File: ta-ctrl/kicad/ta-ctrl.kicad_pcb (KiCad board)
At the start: 4 copper layers, 45 x 45 mm, 0 parts

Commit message: all parts placed, about halfway through routing
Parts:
- added C1: 10nF, ta-ctrl:C_0603_1608Metric_ctrl_cpy, F.Cu at (138.1, 107.4)
- added C10: 100nF, ta-ctrl:C_0603_1608Metric_ctrl_cpy, F.Cu at (159.4, 94.4)
- added C11: 4pF, ta-ctrl:C_0402_1005Metric, F.Cu at (165.2, 100.9)
- added C12: 100nF, ta-ctrl:C_0603_1608Metric_ctrl_cpy, F.Cu at (159.4, 106.9)
- added C13: 4pF, ta-ctrl:C_0402_1005Metric, F.Cu at (163.8, 100.9)
- added C2: 100nF, ta-ctrl:C_0603_1608Metric_ctrl_cpy, F.Cu at (142.5, 107.3)
- added C3: 10uF, ta-ctrl:C_0603_1608Metric_ctrl_cpy, F.Cu at (144.8, 107.3)
- added C4: 100nF, ta-ctrl:C_0603_1608Metric_ctrl_cpy, F.Cu at (140.3, 107.4)
- added C5: 2.2uF, ta-ctrl:C_0603_1608Metric_ctrl_cpy, F.Cu at (172.2, 114.8)
- added C6: 10uF, ta-ctrl:C_0603_1608Metric_ctrl_cpy, F.Cu at (155.6, 92.3)
- added C7: 8pF, ta-ctrl:C_0402_1005Metric, F.Cu at (162.2, 97.2)
- added C8: 100nF, ta-ctrl:C_0603_1608Metric_ctrl_cpy, F.Cu at (148.3, 92.7)
- added C9: 8pF, ta-ctrl:C_0402_1005Metric, F.Cu at (159.6, 90.8)
- added D1: 3.3V, ta-ctrl:D_SOD-323F, F.Cu at (168.8, 102.8)
- added J1: PinSocket_16_ctrl, ta-ctrl:PinSocket_1x16_TartanArtibeus_ctrl_cpy, F.Cu at (155.0, 89.0)
- added J2: PinSocket_16_ctrl, ta-ctrl:PinSocket_1x16_TartanArtibeus_ctrl_cpy, F.Cu at (155.0, 127.0)
- added J3: MountingHole_ctrl, ta-ctrl:MountingHoles_TartanArtibeus_ctrl_cpy, F.Cu at (155.0, 108.0)
- added J4: PinSocket_4_ctrl, ta-ctrl:PinSocket_1x4_TartanArtibeus_ctrl_cpy, F.Cu at (135.9, 120.7)
- added J5: PinSocket_4_ctrl, ta-ctrl:PinSocket_1x4_TartanArtibeus_ctrl_cpy, F.Cu at (135.9, 95.3)
- added J6: PinSocket_5_ctrl, ta-ctrl:PinSocket_1x5_right_TartanArtibeus_ctrl_cpy, F.Cu at (174.1, 122.0)
- added J7: PinSocket_5_ctrl, ta-ctrl:PinSocket_1x5_left_TartanArtibeus_ctrl_cpy, F.Cu at (174.1, 94.0)
- added R1: DNP, ta-ctrl:R_0603_1608Metric_ctrl_cpy, F.Cu at (167.9, 117.4)
- added R10: DNP, ta-ctrl:R_0603_1608Metric_ctrl_cpy, F.Cu at (176.1, 109.0)
- added R11: DNP, ta-ctrl:R_0603_1608Metric_ctrl_cpy, F.Cu at (174.4, 108.9)
- added R12: DNP, ta-ctrl:R_0603_1608Metric_ctrl_cpy, F.Cu at (172.7, 108.9)
- added R13: 10K, ta-ctrl:R_0603_1608Metric_ctrl_cpy, F.Cu at (153.0, 109.7)
- added R14: 10K, ta-ctrl:R_0603_1608Metric_ctrl_cpy, F.Cu at (154.7, 109.7)
- added R15: 10k, ta-ctrl:R_0603_1608Metric_ctrl_cpy, F.Cu at (140.2, 92.7)
- added R16: DNP, ta-ctrl:R_0603_1608Metric_ctrl_cpy, F.Cu at (143.7, 92.7)
- added R17: 10k, ta-ctrl:R_0603_1608Metric_ctrl_cpy, F.Cu at (138.5, 92.7)
- added R18: DNP, ta-ctrl:R_0603_1608Metric_ctrl_cpy, F.Cu at (141.9, 92.7)
- added R19: DNP, ta-ctrl:R_0603_1608Metric_ctrl_cpy, F.Cu at (161.8, 116.5)
- added R2: DNP, ta-ctrl:R_0603_1608Metric_ctrl_cpy, F.Cu at (167.9, 115.8)
- added R3: DNP, ta-ctrl:R_0603_1608Metric_ctrl_cpy, F.Cu at (164.8, 124.9)
- added R4: DNP, ta-ctrl:R_0603_1608Metric_ctrl_cpy, F.Cu at (168.8, 124.9)
- added R5: DNP, ta-ctrl:R_0603_1608Metric_ctrl_cpy, F.Cu at (169.4, 91.6)
- added R6: DNP, ta-ctrl:R_0603_1608Metric_ctrl_cpy, F.Cu at (168.1, 98.8)
- added R7: DNP, ta-ctrl:R_0603_1608Metric_ctrl_cpy, F.Cu at (168.1, 100.4)
- added R8: DNP, ta-ctrl:R_0603_1608Metric_ctrl_cpy, F.Cu at (166.2, 91.6)
- added R9: DNP, ta-ctrl:R_0603_1608Metric_ctrl_cpy, F.Cu at (170.9, 108.9)
- added U1: LSF0204, ta-ctrl:TSSOP-14, F.Cu at (167.8, 121.3)
- added U2: LSF0204, ta-ctrl:TSSOP-14, F.Cu at (168.3, 95.2)
- added U3: LSF0204, ta-ctrl:TSSOP-14, F.Cu at (167.0, 109.2)
- added U4: LSM9DS1, ta-ctrl:LSM9DS1TR, F.Cu at (141.9, 101.2)
- added U5: HT-GPS200.20, ta-ctrl:HT-GPS200.20, F.Cu at (149.5, 116.3)
- added U6: MSP430FR5994IPM, ta-ctrl:MSP430FR5994IPM, F.Cu at (153.7, 100.7)
- added Y1: 32.768kHz, ta-ctrl:ECS327934QSTR, F.Cu at (162.3, 93.3)
- added Y2: 24MHz, ta-ctrl:ECX-1247, F.Cu at (162.2, 101.0)
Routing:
- net /Vdd: track 0.00 -> 134.2 mm, vias 0 -> 8
- net /EXP: track 0.00 -> 50.9 mm, vias 0 -> 1
- net /GNSS_TX: track 0.00 -> 44.4 mm
- net /GNSS_RX: track 0.00 -> 42.2 mm
- net /COMM: track 0.00 -> 42.2 mm, vias 0 -> 1
- net /Exp_CTS: track 0.00 -> 40.7 mm
- net /GNSS_PPS: track 0.00 -> 39.3 mm
- net /GNSS_nRST: track 0.00 -> 32.9 mm
- net /Comm_RX1_l: track 0.00 -> 30.8 mm, vias 0 -> 2
- net /Exp_TX: track 0.00 -> 30.4 mm
- net /Comm_TX1_l: track 0.00 -> 28.2 mm, vias 0 -> 2
- net /Comm_EN: track 0.00 -> 28.1 mm
- net /GNSS: track 0.00 -> 27.5 mm
- net /Exp_RX_l: track 0.00 -> 25.9 mm, vias 0 -> 2
- net /Exp_TX_l: track 0.00 -> 25.9 mm, vias 0 -> 2
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
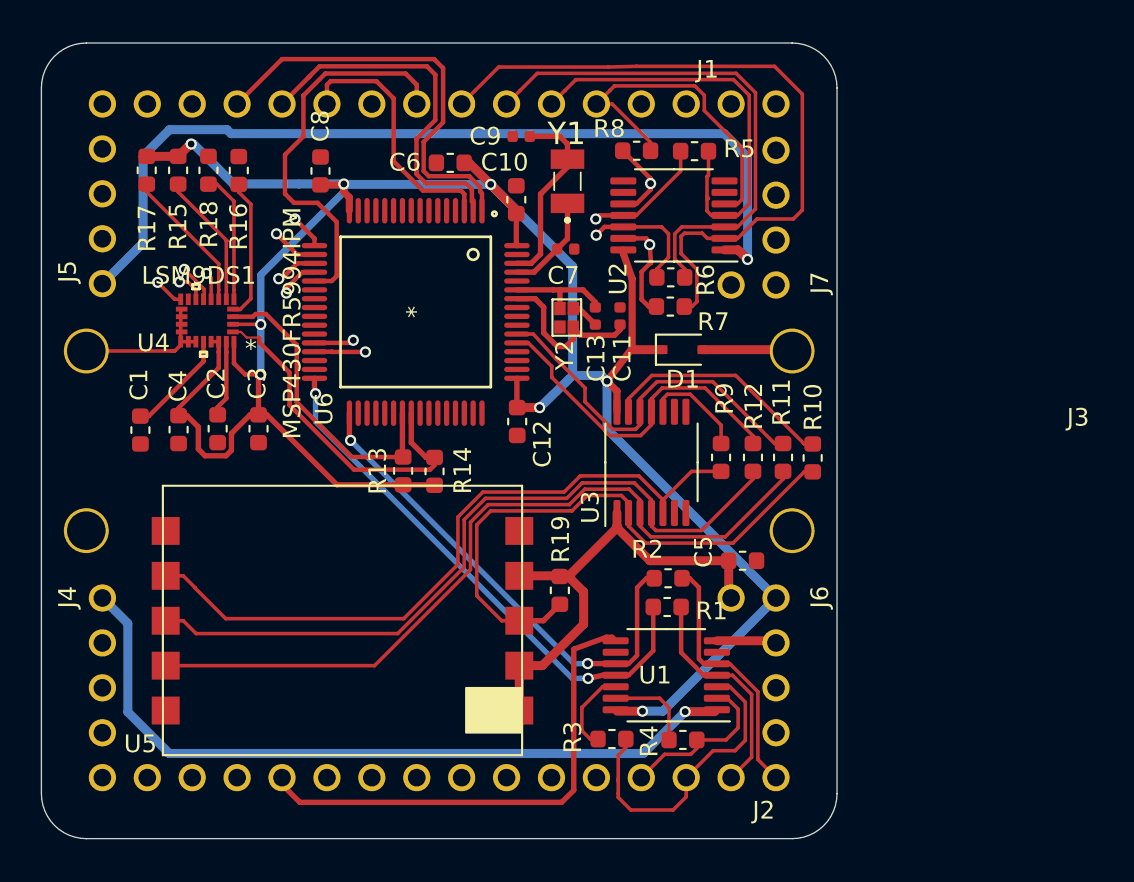
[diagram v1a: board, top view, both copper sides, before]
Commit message: done routing except ground connections
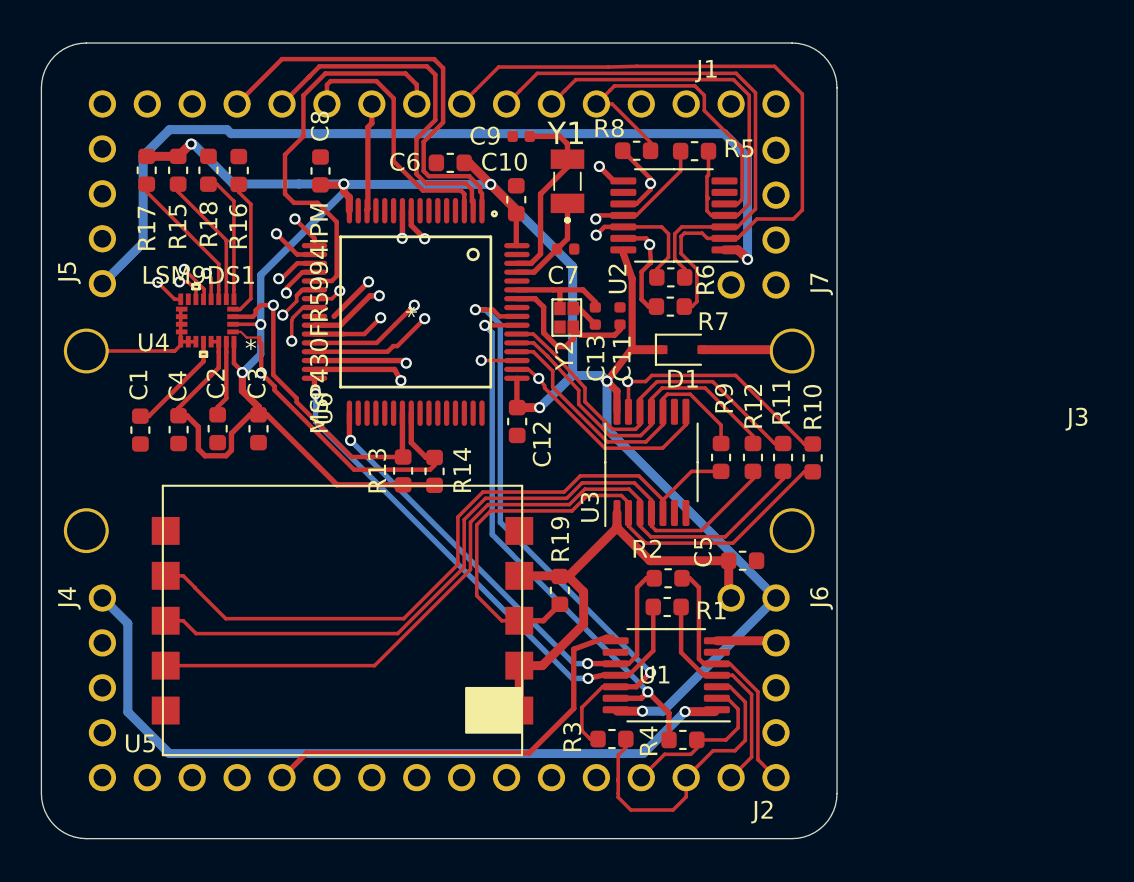
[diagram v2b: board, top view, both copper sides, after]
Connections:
- U6 pad 14: Net-(U6-Pad14) -> /Exp_RST
- U6 pad 22: Net-(U6-Pad22) -> /adc_int
- U6 pad 23: Net-(U6-Pad23) -> /Comm_EN
- U6 pad 24: /EXP_BOOT -> /Exp_EN
- U6 pad 25: /Comm_RST -> Net-(U6-Pad25)
- U6 pad 26: /GNSS_nRST_l -> /Comm_RST
- U6 pad 27: /GNSS_PPS_l -> /EXP_BOOT
- U6 pad 4: /Comm_EN -> Net-(U6-Pad4)
- U6 pad 44: /Exp_RST -> Net-(U6-Pad44)
- U6 pad 5: /Exp_EN -> Net-(U6-Pad5)
- U6 pad 50: Net-(U6-Pad50) -> /Gnss_EN
- U6 pad 51: Net-(U6-Pad51) -> /GNSS_nRST_l
- U6 pad 52: Net-(U6-Pad52) -> /GNSS_PPS_l
- U6 pad 6: /Gnss_EN -> Net-(U6-Pad6)
- U6 pad 7: /adc_int -> Net-(U6-Pad7)
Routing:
- net /Gnss_EN: track 0.00 -> 56.7 mm, vias 0 -> 2
- net /Exp_EN: track 0.00 -> 52.6 mm, vias 0 -> 2
- net /RST: track 0.00 -> 34.9 mm, vias 0 -> 1
- net /TST: track 0.00 -> 33.8 mm, vias 0 -> 1
- net /Comm_RST: track 0.00 -> 33.3 mm, vias 0 -> 1
- net /sda: track 17.4 -> 50.4 mm, vias 0 -> 1
- net /adc_int: track 0.00 -> 31.5 mm, vias 0 -> 1
- net /EXP_BOOT: track 0.00 -> 31.0 mm, vias 0 -> 1
- net /Comm_CTS1_l: track 4.82 -> 34.6 mm, vias 0 -> 2
- net /Comm_EN: track 28.1 -> 54.9 mm, vias 0 -> 1
- net /Comm_RTS1_l: track 5.06 -> 31.6 mm, vias 0 -> 2
- net /scl: track 19.7 -> 45.0 mm, vias 0 -> 1
- net /Exp_CTS_l: track 6.14 -> 24.5 mm, vias 1 -> 2
- net /Exp_RTS_l: track 4.73 -> 20.7 mm, vias 1 -> 2
- net /GNSS_PPS_l: track 5.90 -> 17.9 mm
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
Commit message: ground plane in and 99percent of the way there with silk screen
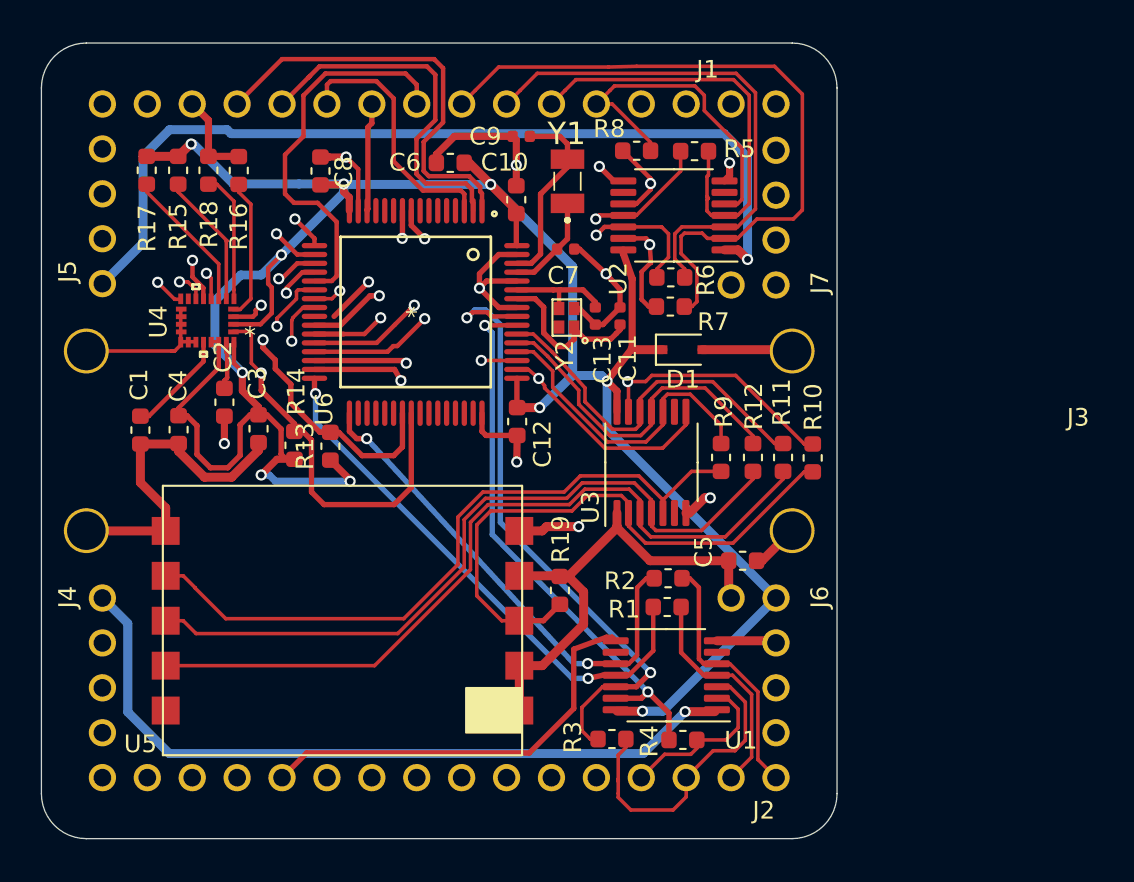
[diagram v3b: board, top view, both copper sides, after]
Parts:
- U4: footprint ta-ctrl:LSM9DS1TR -> ta-ctrl:LSM9DS1TRL
- moved R14 8.06 mm to (146.8, 108.3)
- moved R13 4.35 mm to (148.8, 108.3)
- moved C2 1.55 mm to (142.8, 105.8)
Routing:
- net GND: track 18.5 -> 85.1 mm, vias 0 -> 9
- net /Vdd: track 134.1 -> 143.2 mm, vias 8 -> 10
- net /scl: track 45.0 -> 50.3 mm
- net /MCU/DEN_AG: track 13.4 -> 15.6 mm
- net Net-(C2-Pad1): track 4.34 -> 2.75 mm
- net /sda: track 50.4 -> 48.8 mm, vias 1 -> 2
- net /Comm_CTS1_l: track 34.6 -> 35.8 mm
- net /MCU/INT_AG: track 11.9 -> 13.1 mm
- added copper zone on In1.Cu, net GND
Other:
- net class Default: clearance 0.1524 -> 0.127
- rule trace_clearance: 0.1524 -> 0.127

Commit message: Gerbers for control board
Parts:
- added R20: DNP, ta-ctrl:R_0603_1608Metric_ctrl_cpy, F.Cu at (162.0, 115.0)
- added R21: DNP, ta-ctrl:R_0603_1608Metric_ctrl_cpy, F.Cu at (164.2, 115.1)
- moved R19 1.91 mm to (162.0, 118.4), turned to 90 degrees
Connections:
- U5 pad 4: /GNSS -> /Sensors/Vbackup
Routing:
- net /Vdd: track 143.2 -> 150.3 mm, vias 10 -> 11
- net /Sensors/Vbackup: track 0.00 -> 4.74 mm
- net /GNSS: track 27.5 -> 26.9 mm
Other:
- board text added: "CK"
- board text added: "CO"
- board text added: "CTS"
- board text added: "Co. pins"
- board text added: "EXP"
- board text added: "Exp. pins"
- board text added: "GPS"
- board text added: "RST"
- board text added: "RTS"
- board text added: "RX"
- board text added: "TA CTRL v0.0 2020"
- board text added: "TST"
- board text added: "TX"
- board text added: "Vdd"
- board text added: "adc"
- board text added: "co en"
- board text added: "co rst"
- board text added: "db0"
- board text added: "db1"
- board text added: "db2"
- board text added: "exp boot"
- board text added: "exp en"
- board text added: "gnd"
- board text added: "gps en"
- board text added: "scl"
- board text added: "sda"

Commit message: updated gerbers
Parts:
- added G***: LOGO, ta-ctrl:artibeus-logo, B.Cu at (155.0, 108.0)

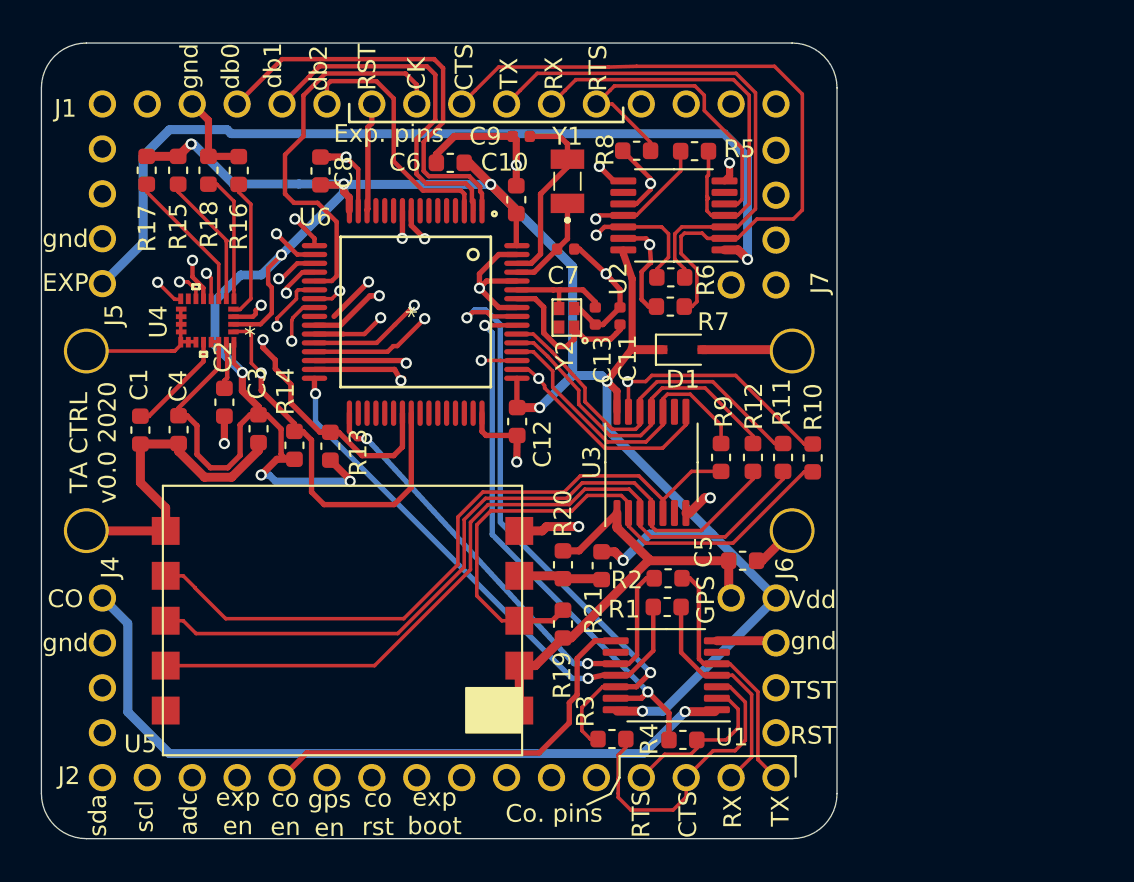
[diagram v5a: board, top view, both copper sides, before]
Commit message: deleted fp-info-cache files???
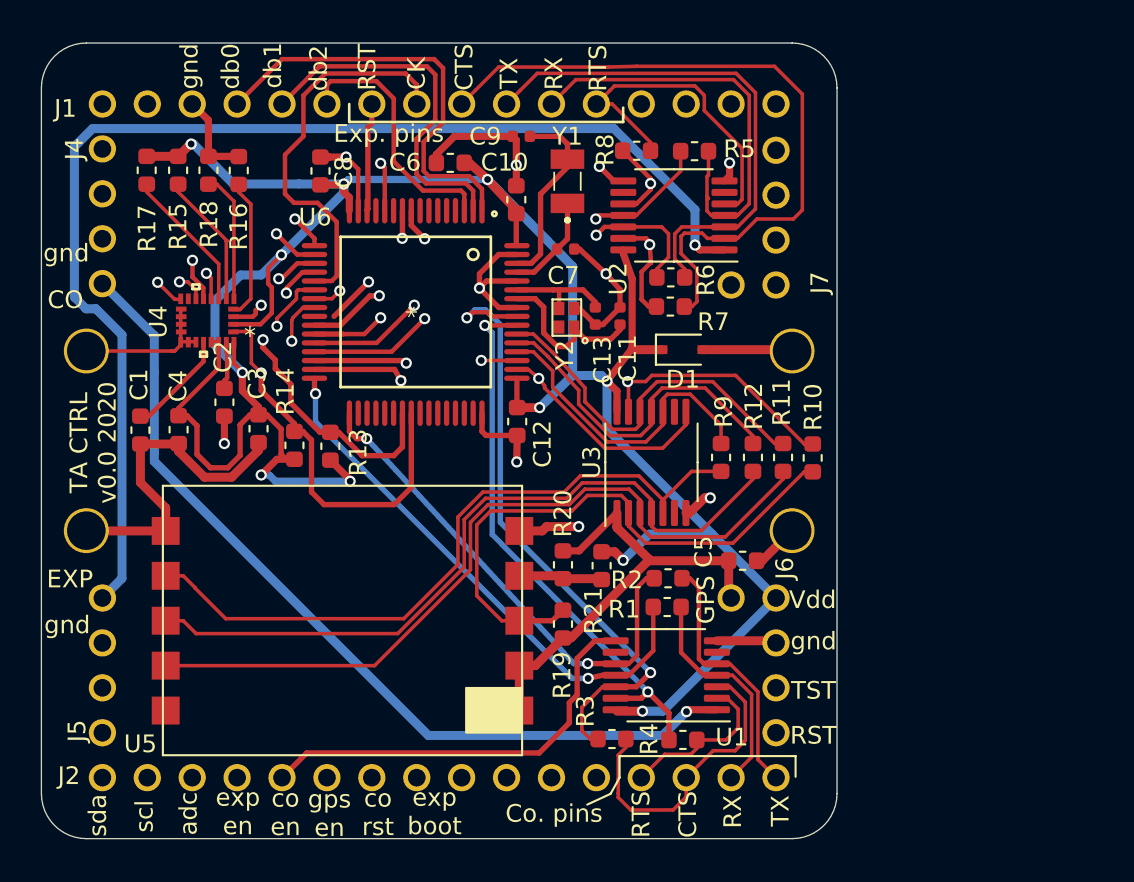
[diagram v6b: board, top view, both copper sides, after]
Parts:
- removed G***: LOGO, ta-ctrl:artibeus-logo
- R13, R14: value 10K -> 10k
- moved J4 25.4 mm to (135.9, 95.3), turned to 0 degrees
- moved J5 25.4 mm to (135.9, 120.7), turned to 180 degrees
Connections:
- J1 pad 2: Net-(J1-Pad2) -> /BURN
- U6 pad 12: Net-(U6-Pad12) -> /BURN
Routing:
- net /EXP: track 50.9 -> 68.6 mm
- net /BURN: track 0.00 -> 17.6 mm, vias 0 -> 1
- net /COMM: track 42.2 -> 50.1 mm

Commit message: updated ctrl and pwr
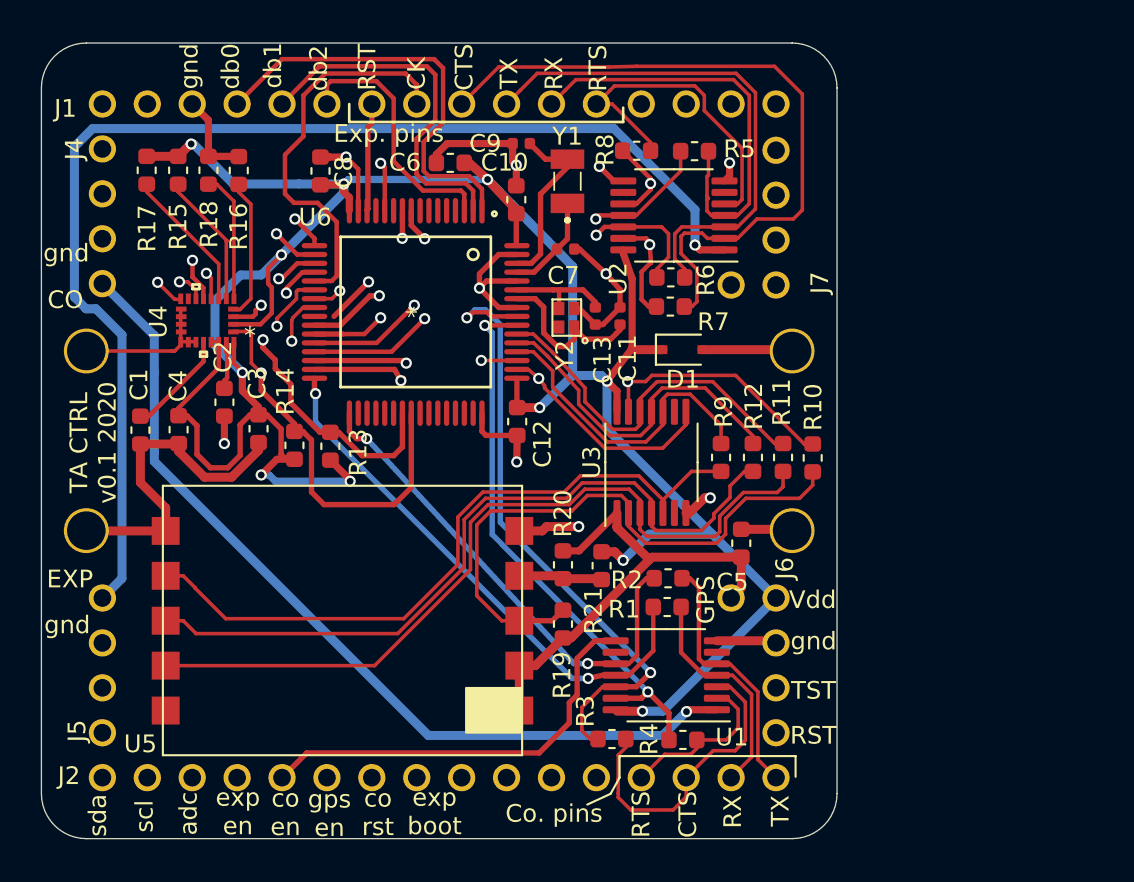
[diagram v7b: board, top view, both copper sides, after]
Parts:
- moved C5 0.99 mm to (172.1, 113.8), turned to 90 degrees
- moved C9 0.41 mm to (159.6, 91.2)
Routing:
- net /GNSS_nRST: track 33.0 -> 35.1 mm
- net /GNSS: track 26.9 -> 28.2 mm
- net /GNSS_TX: track 44.4 -> 45.3 mm
- net Net-(C9-Pad1): track 10.7 -> 10.0 mm
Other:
- board text added: "TA CTRL v0.1 2020"
- board text removed: "TA CTRL v0.0 2020"
